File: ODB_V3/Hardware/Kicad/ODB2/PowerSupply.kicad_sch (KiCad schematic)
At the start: 49 parts, among them J15 Vin_XT30PW-F, U13 L6981N33DR, U7 MPQ9843GLE-5-AEC1-Z

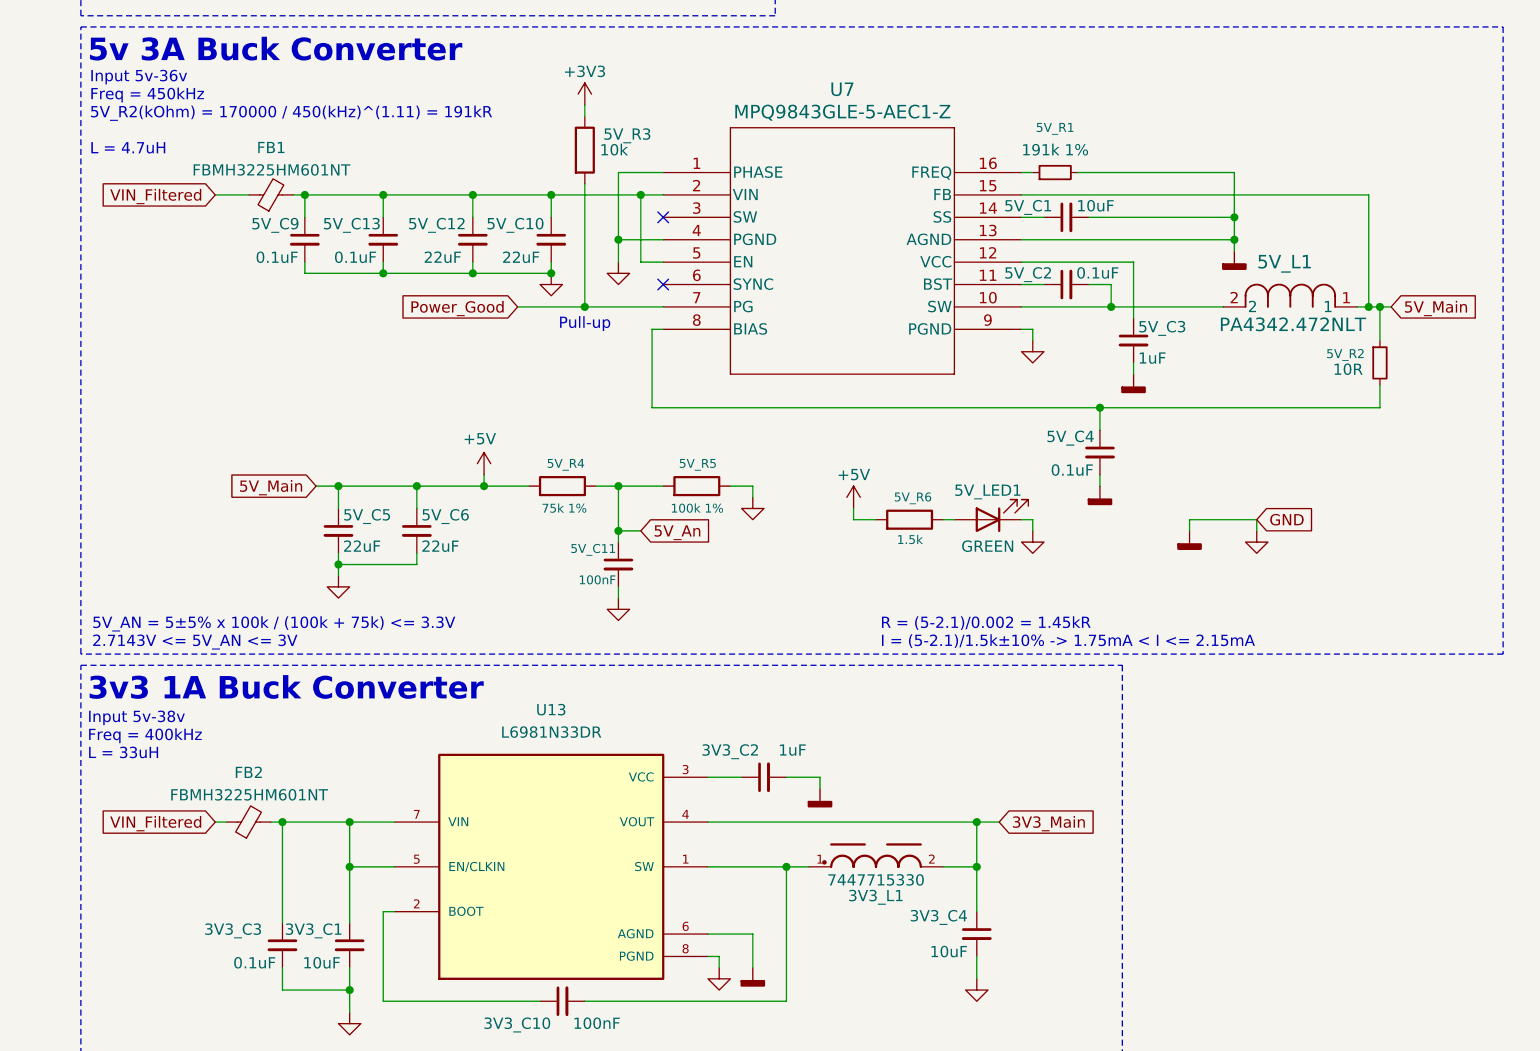
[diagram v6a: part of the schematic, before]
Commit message: wip : digikey part number et lien pour toutes pièces importantes (pas résistances, capacités, etc)
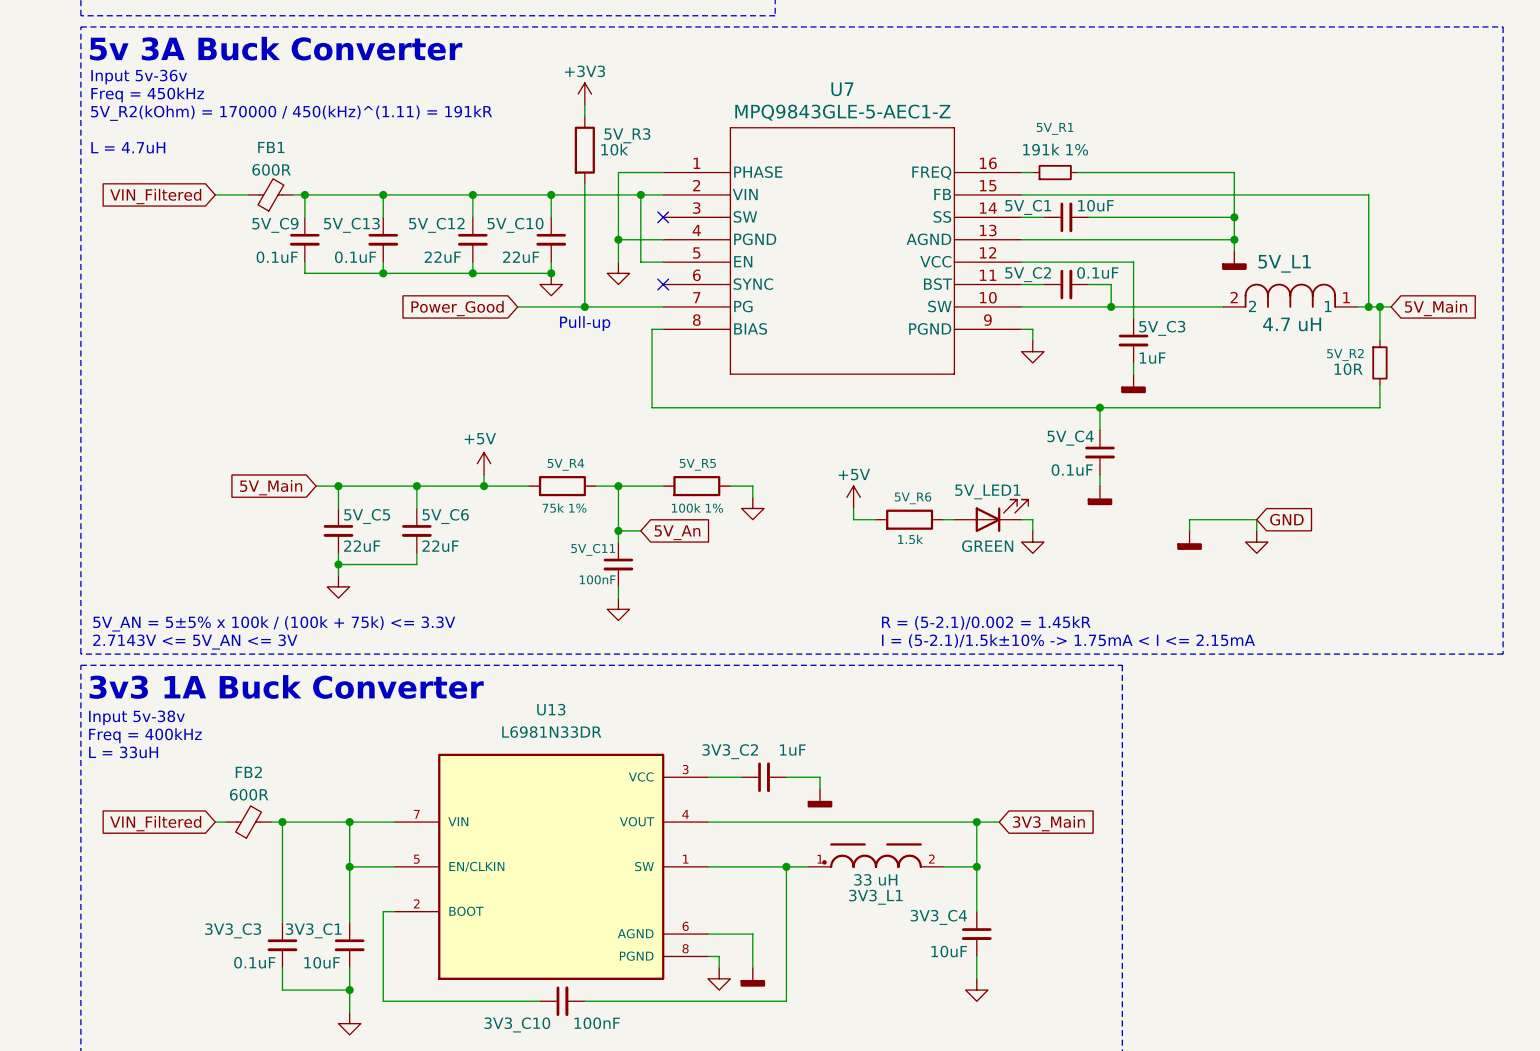
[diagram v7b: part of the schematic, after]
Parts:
- 3V3_L1: value 7447715330 -> 33 uH; DigiKey_Part_Number (none) -> 732-2196-1-ND; Digikey (none) -> 732-2196-1-ND
- 5V_L1: value PA4342.472NLT -> 4.7 uH; DigiKey_Part_Number (none) -> 553-3001-1-ND; Digikey (none) -> 553-3001-1-ND
- FB1, FB2: value FBMH3225HM601NT -> 600R; DigiKey_Part_Number (none) -> 587-1755-1-ND
- U13: DigiKey_Part_Number (none) -> 497-L6981N33DRCT-ND
- U7: DigiKey_Part_Number (none) -> 1589-MPQ9843GLE-5-AEC1-ZCT-ND
- Vin_C4: DigiKey_Part_Number (none) -> 732-11942-1-ND
- Vin_F1: DigiKey_Part_Number (none) -> 18-2920L700/24SLERCT-ND
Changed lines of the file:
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@@
 			)
 		)
-		(property "Value" "PA4342.472NLT"
+		(property "Value" "4.7 uH"
 			(at 152.654 85.852 0)
 			(effects
@@
 			)
 		)
-		(property "Datasheet" "PA4342.472NLT"
+		(property "Datasheet" "https://www.digikey.ca/en/products/detail/pulse-electronics/PA4342-472NLT/5436333"
 			(at 144.78 83.82 0)
 			(effects
@@
 			)
 		)
-		(property "Description" ""
+		(property "Description" "4.7 µH Shielded Molded Inductor 10 A 15.5mOhm Max Nonstandard"
 			(at 144.78 83.82 0)
 			(effects
@@
 			)
 		)
-		(property "DigiKey_Part_Number" ""
+		(property "Digikey" "553-3001-1-ND"
 			(at 144.78 83.82 0)
 			(effects
@@
 			)
 		)
+		(property "DigiKey_Part_Number" "553-3001-1-ND"
+			(at 144.78 83.82 0)
+			(effects
+				(font
+					(size 1.27 1.27)
+				)
+				(hide yes)
+			)
+		)
 		(pin "2"
 		)
@@
 			)
 		)
-		(property "Value" "7447715330"
+		(property "Value" "33 uH"
 			(at 105.41 148.844 0)
 			(effects
@@
 			)
 		)
-		(property "Datasheet" ""
+		(property "Datasheet" "https://www.digikey.ca/en/products/detail/w%C3%BCrth-elektronik/7447715330/2175612"
 			(at 105.41 147.32 0)
 			(effects
@@
 			)
 		)
-		(property "Description" ""
+		(property "Description" "7447715330; 33 µH Shielded Drum Core, Wirewound Inductor 2.3 A 85mOhm Max Nonstandard"
 			(at 105.41 147.32 0)
 			(effects
@@
 			)
 		)
-		(property "DigiKey_Part_Number" ""
+		(property "Digikey" "732-2196-1-ND"
 			(at 105.41 147.32 0)
 			(effects
@@
 			)
 		)
+		(property "DigiKey_Part_Number" "732-2196-1-ND"
+			(at 105.41 147.32 0)
+			(effects
+				(font
+					(size 1.27 1.27)
+				)
+				(hide yes)
+			)
+		)
 		(pin "1"
 		)
@@
 			)
 		)
-		(property "DigiKey_Part_Number" ""
+		(property "DigiKey_Part_Number" "732-11942-1-ND"
 			(at 21.59 38.1 0)
 			(effects
@@
 			)
 		)
-		(property "Datasheet" "https://www.monolithicpower.com/en/documentview/productdocument/index/version/2/document_type/Datasheet/lang/en/sku/MPQ9843GL"
+		(property "Datasheet" "https://www.digikey.com/en/products/detail/monolithic-power-systems-inc/MPQ9843GLE-5-AEC1-Z/14645612"
 			(at 81.28 68.58 0)
 			(effects
@@
 			)
 		)
-		(property "DigiKey_Part_Number" ""
+		(property "DigiKey_Part_Number" "1589-MPQ9843GLE-5-AEC1-ZCT-ND"
 			(at 81.28 68.58 0)
 			(effects
@@
 			)
 		)
-		(property "Datasheet" "2920L700/24SLER"
+		(property "Datasheet" "https://www.digikey.ca/en/products/detail/littelfuse-inc/2920L700-24SLER/12807015"
 			(at 257.81 27.94 0)
 			(effects
@@
 			)
 		)
-		(property "DigiKey_Part_Number" ""
+		(property "DigiKey_Part_Number" "18-2920L700/24SLERCT-ND"
 			(at 257.81 27.94 90)
 			(effects
@@
 			)
 		)
-		(property "Datasheet" ""
+		(property "Datasheet" "https://www.digikey.com/en/products/detail/stmicroelectronics/L6981N33DR/16841571"
 			(at 68.58 147.32 0)
 			(effects
@@
 			)
 		)
-		(property "DigiKey_Part_Number" ""
+		(property "DigiKey_Part_Number" "497-L6981N33DRCT-ND"
 			(at 68.58 147.32 0)
 			(effects
@@
 			)
 		)
-		(property "Value" "FBMH3225HM601NT"
+		(property "Value" "600R"
 			(at 36.83 68.326 90)
 			(effects
@@
 			)
 		)
-		(property "Datasheet" "~"
+		(property "Datasheet" "https://www.digikey.ca/en/products/detail/taiyo-yuden/FBMH3225HM601NT/957843"
 			(at 36.83 71.12 0)
 			(effects
@@
 			)
 		)
-		(property "Description" "Ferrite bead, small symbol"
+		(property "Description" "600 Ohms @ 100 MHz 1 Power Line Ferrite Bead 1210 (3225 Metric) 3A 42mOhm"
 			(at 36.83 71.12 0)
 			(effects
@@
 			)
 		)
-		(property "DigiKey_Part_Number" ""
+		(property "DigiKey_Part_Number" "587-1755-1-ND"
 			(at 36.83 71.12 90)
 			(effects
@@
 			)
 		)
-		(property "Value" "FBMH3225HM601NT"
+		(property "Value" "600R"
 			(at 34.29 139.192 90)
 			(effects
@@
 			)
 		)
-		(property "Datasheet" "~"
+		(property "Datasheet" "https://www.digikey.ca/en/products/detail/taiyo-yuden/FBMH3225HM601NT/957843"
 			(at 34.29 142.24 0)
 			(effects
@@
 			)
 		)
-		(property "Description" "Ferrite bead, small symbol"
+		(property "Description" "600 Ohms @ 100 MHz 1 Power Line Ferrite Bead 1210 (3225 Metric) 3A 42mOhm"
 			(at 34.29 142.24 0)
 			(effects
@@
 			)
 		)
-		(property "DigiKey_Part_Number" ""
+		(property "DigiKey_Part_Number" "587-1755-1-ND"
 			(at 34.29 142.24 90)
 			(effects

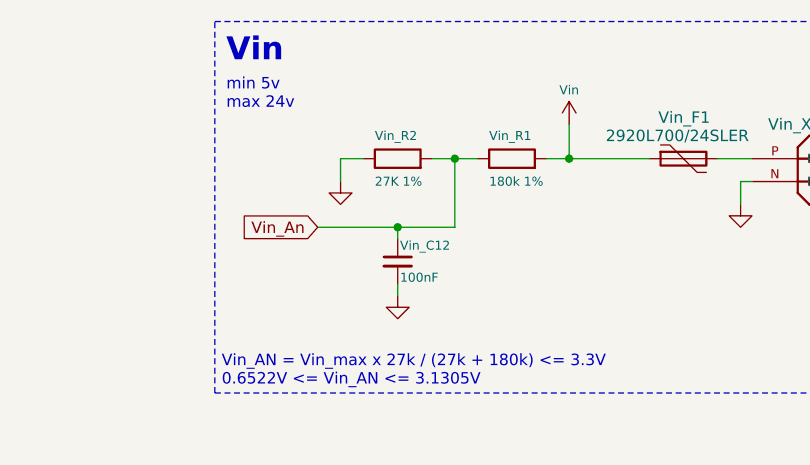
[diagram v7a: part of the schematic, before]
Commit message: fix : change pieces and footprints to reduce BOM
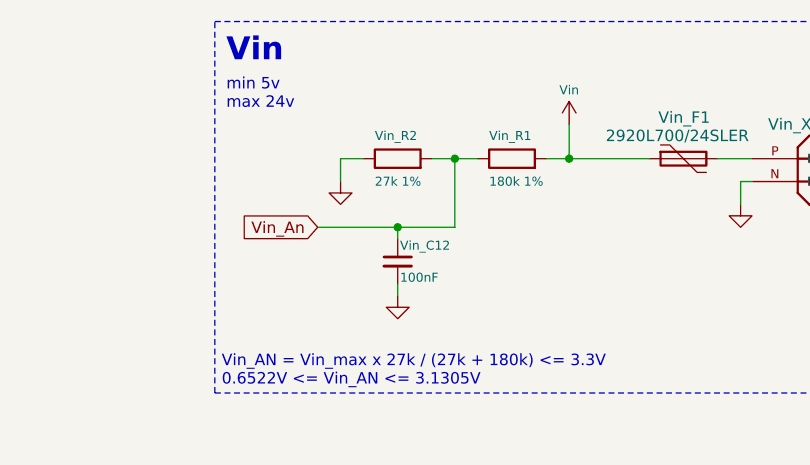
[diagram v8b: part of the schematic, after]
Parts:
- Vin_R2: value 27K 1% -> 27k 1%
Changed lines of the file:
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@@
 			)
 		)
-		(property "Value" "27K 1%"
+		(property "Value" "27k 1%"
 			(at 223.52 30.48 90)
 			(effects
